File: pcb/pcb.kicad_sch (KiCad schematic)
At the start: 0 parts

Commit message: feat: added flash
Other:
- added sheet [1] Power Delivery (pd.kicad_sch)
- added sheet [2] System (system.kicad_sch)
- added sheet [3] Sensors (sensors.kicad_sch)
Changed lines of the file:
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@@
 	(generator_version "9.0")
 	(paper "A4")
+	(sheet
+		(at 93.98 92.71)
+		(size 67.31 35.56)
+		(exclude_from_sim no)
+		(in_bom yes)
+		(on_board yes)
+		(dnp no)
+		(fields_autoplaced yes)
+		(stroke
+			(width 0.1524)
+			(type solid)
+		)
+		(fill
+			(color 0 0 0 0.0000)
+		)
+		(property "Sheetname" "[3] Sensors"
+			(at 93.98 91.9984 0)
+			(effects
+				(font
+					(size 1.27 1.27)
+				)
+				(justify left bottom)
+			)
+		)
+		(property "Sheetfile" "sensors.kicad_sch"
+			(at 93.98 128.8546 0)
+			(effects
+				(font
+					(size 1.27 1.27)
+				)
+				(justify left top)
+			)
+		)
+		(instances
+			(project "pcb"
+				(path "/9bba97c2-2e09-46fb-bf2a-7de104403c7c"
+					(page "4")
+				)
+			)
+		)
+	)
+	(sheet
+		(at 53.34 43.18)
+		(size 53.34 30.48)
+		(exclude_from_sim no)
+		(in_bom yes)
+		(on_board yes)
+		(dnp no)
+		(fields_autoplaced yes)
+		(stroke
+			(width 0.1524)
+			(type solid)
+		)
+		(fill
+			(color 0 0 0 0.0000)
+		)
+		(property "Sheetname" "[1] Power Delivery"
+			(at 53.34 42.4684 0)
+			(effects
+				(font
+					(size 1.27 1.27)
+				)
+				(justify left bottom)
+			)
+		)
+		(property "Sheetfile" "pd.kicad_sch"
+			(at 53.34 74.2446 0)
+			(effects
+				(font
+					(size 1.27 1.27)
+				)
+				(justify left top)
+			)
+		)
+		(instances
+			(project "pcb"
+				(path "/9bba97c2-2e09-46fb-bf2a-7de104403c7c"
+					(page "2")
+				)
+			)
+		)
+	)
+	(sheet
+		(at 139.7 53.34)
+		(size 60.96 26.67)
+		(exclude_from_sim no)
+		(in_bom yes)
+		(on_board yes)
+		(dnp no)
+		(fields_autoplaced yes)
+		(stroke
+			(width 0.1524)
+			(type solid)
+		)
+		(fill
+			(color 0 0 0 0.0000)
+		)
+		(property "Sheetname" "[2] System"
+			(at 139.7 52.6284 0)
+			(effects
+				(font
+					(size 1.27 1.27)
+				)
+				(justify left bottom)
+			)
+		)
+		(property "Sheetfile" "system.kicad_sch"
+			(at 139.7 80.5946 0)
+			(effects
+				(font
+					(size 1.27 1.27)
+				)
+				(justify left top)
+			)
+		)
+		(instances
+			(project "pcb"
+				(path "/9bba97c2-2e09-46fb-bf2a-7de104403c7c"
+					(page "3")
+				)
+			)
+		)
+	)
 	(sheet_instances
 		(path "/"

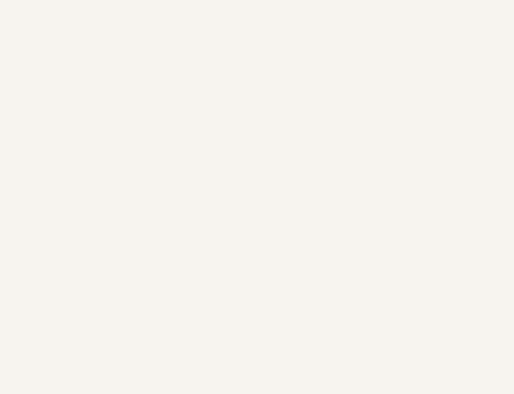
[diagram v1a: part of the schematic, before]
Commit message: chore: mounting holes
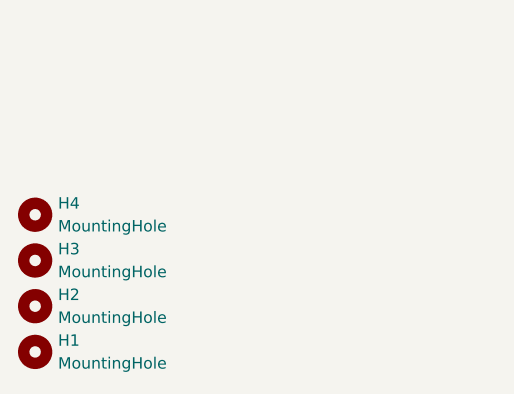
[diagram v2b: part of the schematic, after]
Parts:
- added H1, H2, H3, H4: MountingHole, symbol Mechanical:MountingHole

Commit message: chore: docs
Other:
- company: (none) -> Ivan Leonard O Aparte <ivanleonard.aparte@cit.edu>
- title: (none) -> Schematic Root
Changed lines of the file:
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@@
 	(generator_version "9.0")
 	(paper "A4")
+	(title_block
+		(title "Schematic Root")
+		(date "2026-01-29")
+		(rev "1")
+		(company "Ivan Leonard O Aparte <ivanleonard.aparte@cit.edu>")
+	)
 	(symbol
 		(lib_id "Mechanical:MountingHole")

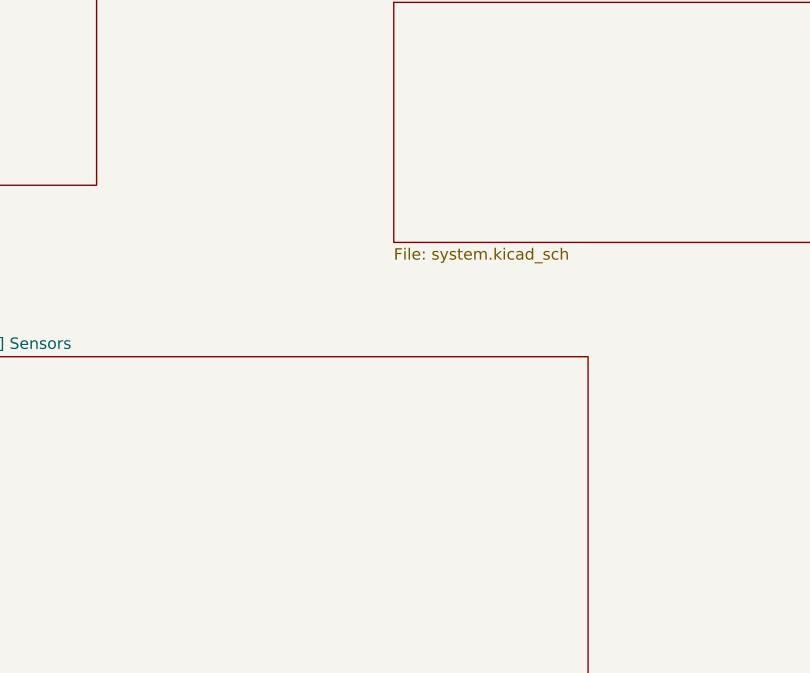
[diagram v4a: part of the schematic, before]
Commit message: chore: added pull-down on rs-485 transceiver
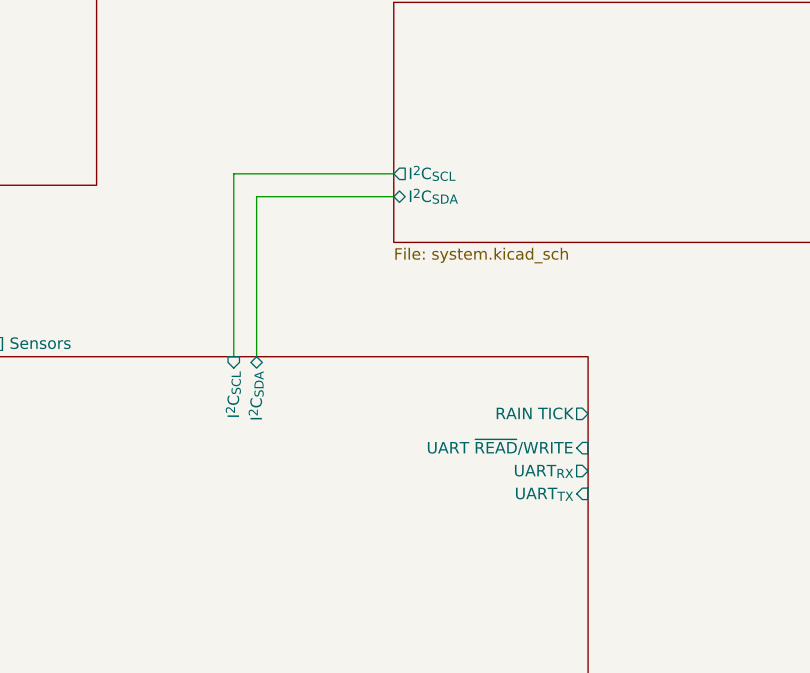
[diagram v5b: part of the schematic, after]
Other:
- sheet [2] System ports: added I^{2}C_{SCL}, I^{2}C_{SDA}; removed none
- sheet [3] Sensors ports: added I^{2}C_{SCL}, I^{2}C_{SDA}, RAIN TICK, UART ~{READ}/WRITE, UART_{RX}, UART_{TX}; removed none
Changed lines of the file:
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@@
 		(company "Ivan Leonard O Aparte <ivanleonard.aparte@cit.edu>")
+	)
+	(wire
+		(pts
+			(xy 124.46 74.93) (xy 124.46 92.71)
+		)
+		(stroke
+			(width 0)
+			(type default)
+		)
+	)
+	(wire
+		(pts
+			(xy 121.92 72.39) (xy 121.92 92.71)
+		)
+		(stroke
+			(width 0)
+			(type default)
+		)
+	)
+	(wire
+		(pts
+			(xy 139.7 72.39) (xy 121.92 72.39)
+		)
+		(stroke
+			(width 0)
+			(type default)
+		)
+	)
+	(wire
+		(pts
+			(xy 139.7 74.93) (xy 124.46 74.93)
+		)
+		(stroke
+			(width 0)
+			(type default)
+		)
 	)
 	(symbol
@@
 			)
 		)
+		(pin "I^{2}C_{SCL}" input
+			(at 121.92 92.71 90)
+			(effects
+				(font
+					(size 1.27 1.27)
+				)
+				(justify right)
+			)
+		)
+		(pin "I^{2}C_{SDA}" bidirectional
+			(at 124.46 92.71 90)
+			(effects
+				(font
+					(size 1.27 1.27)
+				)
+				(justify right)
+			)
+		)
+		(pin "RAIN TICK" output
+			(at 161.29 99.06 0)
+			(effects
+				(font
+					(size 1.27 1.27)
+				)
+				(justify right)
+			)
+		)
+		(pin "UART ~{READ}{slash}WRITE" input
+			(at 161.29 102.87 0)
+			(effects
+				(font
+					(size 1.27 1.27)
+				)
+				(justify right)
+			)
+		)
+		(pin "UART_{RX}" output
+			(at 161.29 105.41 0)
+			(effects
+				(font
+					(size 1.27 1.27)
+				)
+				(justify right)
+			)
+		)
+		(pin "UART_{TX}" input
+			(at 161.29 107.95 0)
+			(effects
+				(font
+					(size 1.27 1.27)
+				)
+				(justify right)
+			)
+		)
 		(instances
 			(project "pcb"
@@
 			)
 		)
+		(pin "I^{2}C_{SCL}" output
+			(at 139.7 72.39 180)
+			(effects
+				(font
+					(size 1.27 1.27)
+				)
+				(justify left)
+			)
+		)
+		(pin "I^{2}C_{SDA}" bidirectional
+			(at 139.7 74.93 180)
+			(effects
+				(font
+					(size 1.27 1.27)
+				)
+				(justify left)
+			)
+		)

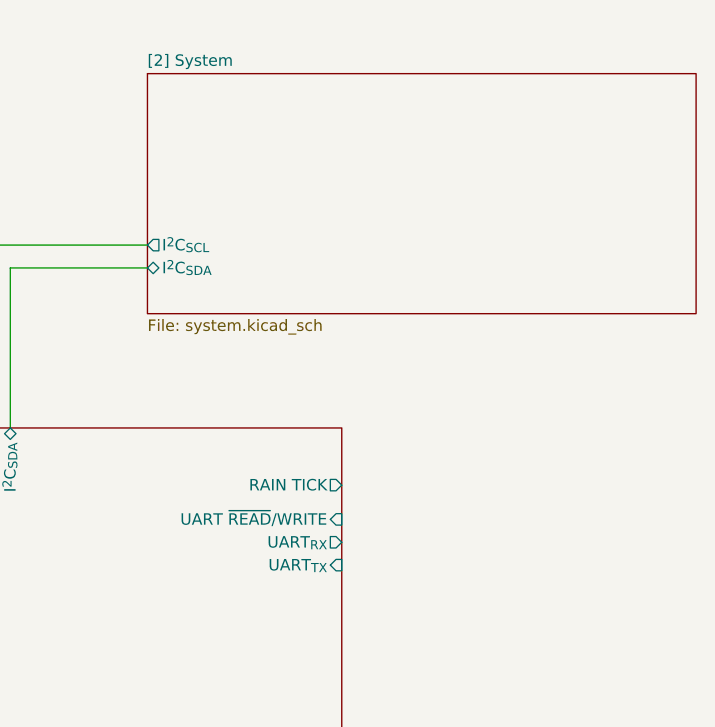
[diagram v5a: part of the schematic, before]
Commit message: feat: pin layout for I2C, SPI, and UART peripherals
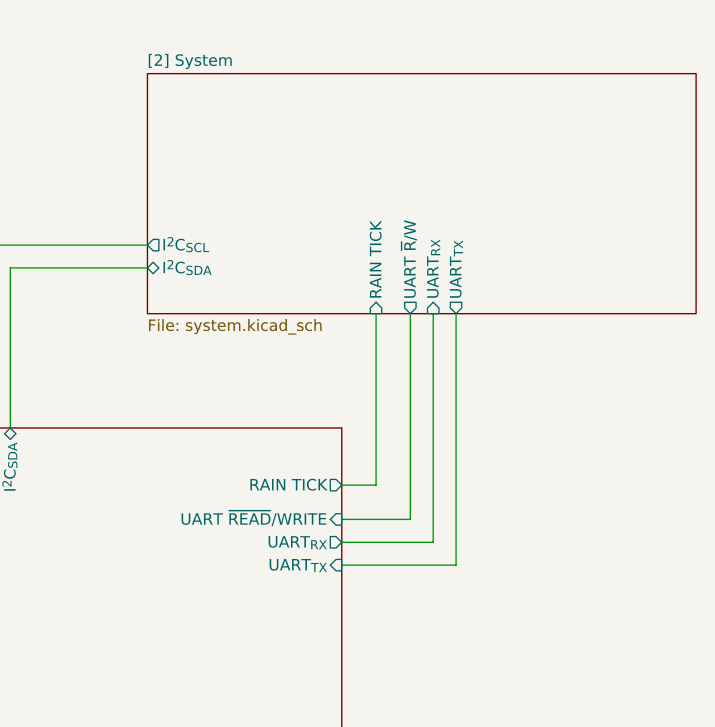
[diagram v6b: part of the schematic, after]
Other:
- sheet [2] System ports: added RAIN TICK, UART ~{R}/W, UART_{RX}, UART_{TX}; removed none
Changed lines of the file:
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@@
+	(wire
+		(pts
+			(xy 173.99 107.95) (xy 161.29 107.95)
+		)
+		(stroke
+			(width 0)
+			(type default)
+		)
+	)
+	(wire
+		(pts
+			(xy 165.1 99.06) (xy 161.29 99.06)
+		)
+		(stroke
+			(width 0)
+			(type default)
+		)
+	)
+	(wire
+		(pts
+			(xy 171.45 80.01) (xy 171.45 105.41)
+		)
+		(stroke
+			(width 0)
+			(type default)
+		)
+	)
+	(wire
+		(pts
+			(xy 171.45 105.41) (xy 161.29 105.41)
+		)
+		(stroke
+			(width 0)
+			(type default)
+		)
+	)
+	(wire
+		(pts
+			(xy 168.91 80.01) (xy 168.91 102.87)
+		)
+		(stroke
+			(width 0)
+			(type default)
+		)
+	)
+	(wire
+		(pts
+			(xy 168.91 102.87) (xy 161.29 102.87)
+		)
+		(stroke
+			(width 0)
+			(type default)
+		)
+	)
+	(wire
+		(pts
+			(xy 165.1 80.01) (xy 165.1 99.06)
+		)
+		(stroke
+			(width 0)
+			(type default)
+		)
+	)
+	(wire
+		(pts
+			(xy 173.99 80.01) (xy 173.99 107.95)
+		)
+		(stroke
+			(width 0)
+			(type default)
+		)
+	)
 	(wire
 		(pts
@@
 			(effects
 				(font
+					(size 1.27 1.27)
+				)
+				(justify left)
+			)
+		)
+		(pin "RAIN TICK" input
+			(at 165.1 80.01 270)
+			(effects
+				(font
+					(size 1.27 1.27)
+				)
+				(justify left)
+			)
+		)
+		(pin "UART ~{R}{slash}W" output
+			(at 168.91 80.01 270)
+			(effects
+				(font
+					(size 1.27 1.27)
+				)
+				(justify left)
+			)
+		)
+		(pin "UART_{RX}" input
+			(at 171.45 80.01 270)
+			(effects
+				(font
+					(size 1.27 1.27)
+				)
+				(justify left)
+			)
+		)
+		(pin "UART_{TX}" output
+			(at 173.99 80.01 270)
+			(effects
+				(font

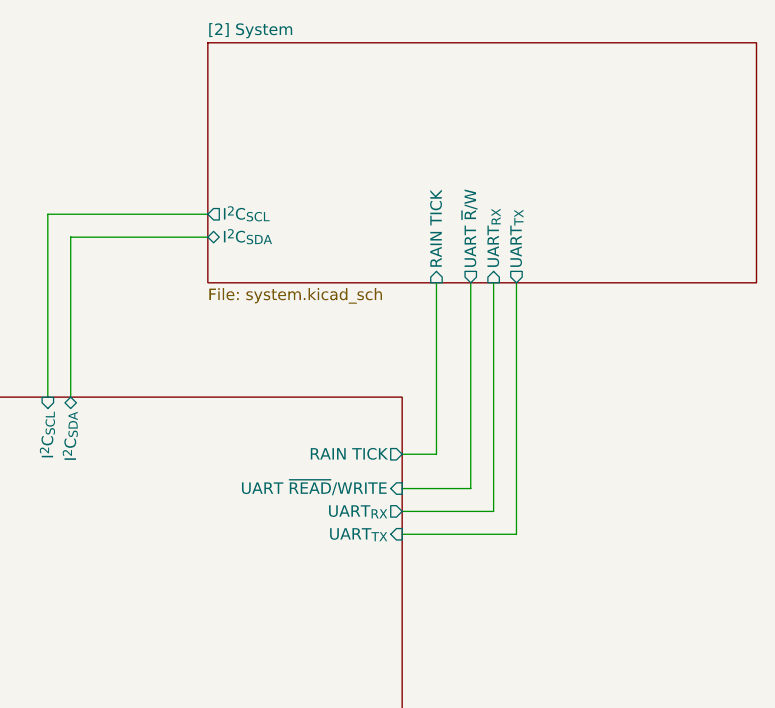
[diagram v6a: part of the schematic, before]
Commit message: feat: PMS7003 sensor
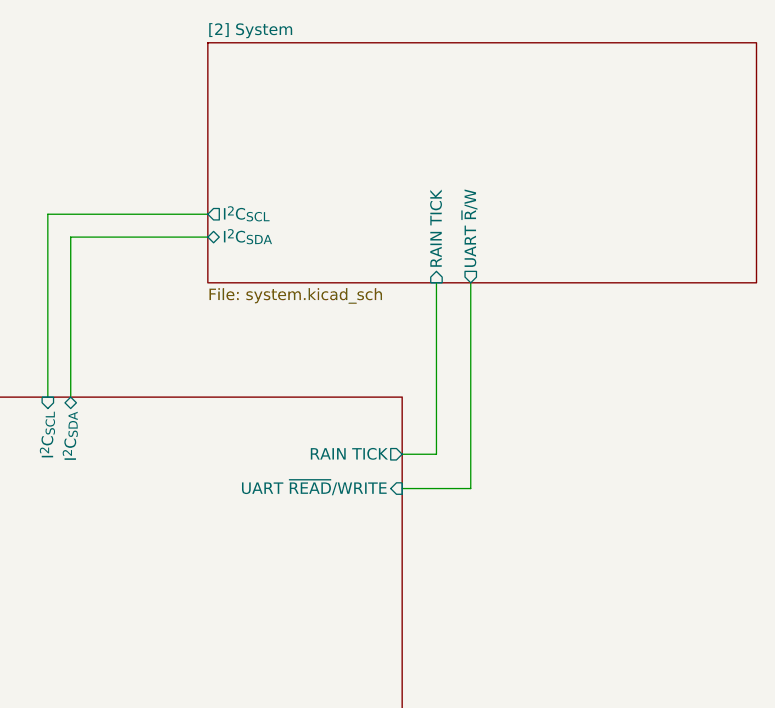
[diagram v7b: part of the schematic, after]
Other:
- sheet [2] System ports: added none; removed UART_{RX}, UART_{TX}
- sheet [3] Sensors ports: added none; removed UART_{RX}, UART_{TX}
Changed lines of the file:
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@@
-	(wire
-		(pts
-			(xy 173.99 107.95) (xy 161.29 107.95)
-		)
-		(stroke
-			(width 0)
-			(type default)
-		)
-	)
 	(wire
 		(pts
@@
 	(wire
 		(pts
-			(xy 171.45 80.01) (xy 171.45 105.41)
-		)
-		(stroke
-			(width 0)
-			(type default)
-		)
-	)
-	(wire
-		(pts
-			(xy 171.45 105.41) (xy 161.29 105.41)
-		)
-		(stroke
-			(width 0)
-			(type default)
-		)
-	)
-	(wire
-		(pts
 			(xy 168.91 80.01) (xy 168.91 102.87)
 		)
@@
 		(pts
 			(xy 165.1 80.01) (xy 165.1 99.06)
-		)
-		(stroke
-			(width 0)
-			(type default)
-		)
-	)
-	(wire
-		(pts
-			(xy 173.99 80.01) (xy 173.99 107.95)
 		)
 		(stroke
@@
 			)
 		)
-		(pin "UART_{RX}" output
-			(at 161.29 105.41 0)
-			(effects
-				(font
-					(size 1.27 1.27)
-				)
-				(justify right)
-			)
-		)
-		(pin "UART_{TX}" input
-			(at 161.29 107.95 0)
-			(effects
-				(font
-					(size 1.27 1.27)
-				)
-				(justify right)
-			)
-		)
 		(instances
 			(project "pcb"
@@
 			(effects
 				(font
-					(size 1.27 1.27)
-				)
-				(justify left)
-			)
-		)
-		(pin "UART_{RX}" input
-			(at 171.45 80.01 270)
-			(effects
-				(font
-					(size 1.27 1.27)
-				)
-				(justify left)
-			)
-		)
-		(pin "UART_{TX}" output
-			(at 173.99 80.01 270)
-			(effects
-				(font

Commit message: chore: date update
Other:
- title: Schematic Root -> Banshee Microcontroller + Supporting Systems
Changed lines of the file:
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@@
 	(paper "A4")
 	(title_block
-		(title "Schematic Root")
-		(date "2026-01-29")
+		(title "Banshee Microcontroller + Supporting Systems")
+		(date "2026-02-05")
 		(rev "1")
 		(company "Ivan Leonard O Aparte <ivanleonard.aparte@cit.edu>")
